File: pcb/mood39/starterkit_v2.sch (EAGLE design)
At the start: 18 parts, among them IC1 TINY85, IC2 LM2940, X1 PWRUSB

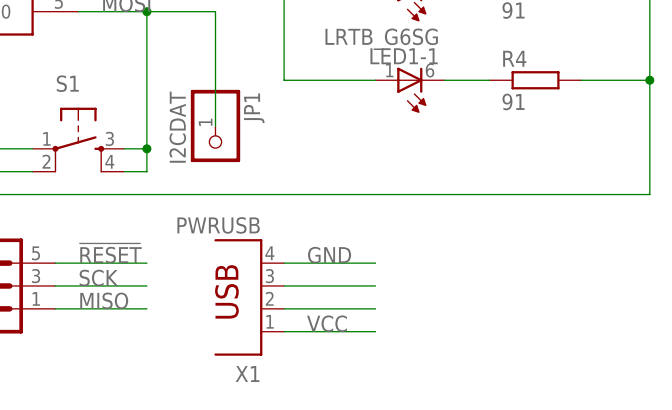
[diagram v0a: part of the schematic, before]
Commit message: add pins for USB data
those pins can be used for actually accessing the avr via USB, but it
needs some additional circuit stacked on the pin headers
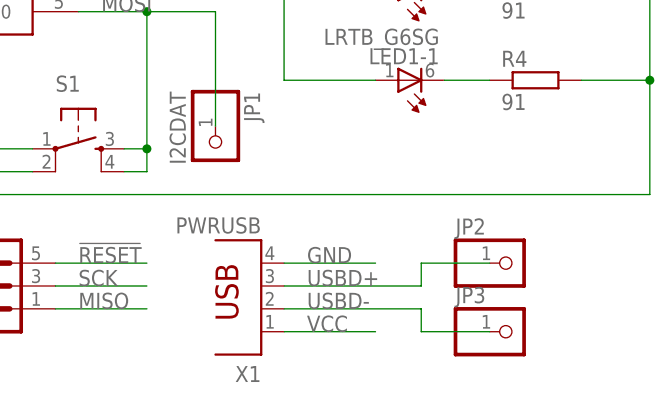
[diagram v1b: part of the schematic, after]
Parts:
- added JP2, JP3: (no value), pinhead:PINHD-1X1
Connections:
- net USBD+: now also JP2.1
- net USBD-: now also JP3.1
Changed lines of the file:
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@@
 <?xml version="1.0" encoding="utf-8"?>
 <!DOCTYPE eagle SYSTEM "eagle.dtd">
-<eagle version="6.4">
+<eagle version="6.5.0">
 <drawing>
 <settings>
@@
 <part name="S1" library="n39" deviceset="JTP-1130" device="" technology="C" value=""/>
 <part name="U$1" library="n39" deviceset="RIACON_101_2" device=""/>
+<part name="JP2" library="pinhead" deviceset="PINHD-1X1" device=""/>
+<part name="JP3" library="pinhead" deviceset="PINHD-1X1" device=""/>
 </parts>
 <sheets>
@@
 <instance part="S1" gate="S$1" x="73.66" y="50.8" rot="R270"/>
 <instance part="U$1" gate="G$1" x="-30.48" y="88.9" rot="R180"/>
+<instance part="JP2" gate="G$1" x="121.92" y="38.1"/>
+<instance part="JP3" gate="G$1" x="121.92" y="30.48"/>
 </instances>
 <busses>
@@
 <segment>
 <pinref part="X1" gate="G$1" pin="2"/>
-<wire x1="96.52" y1="33.02" x2="106.68" y2="33.02" width="0.1524" layer="91"/>
+<wire x1="96.52" y1="33.02" x2="111.76" y2="33.02" width="0.1524" layer="91"/>
+<label x="99.06" y="33.02" size="1.778" layer="95"/>
+<pinref part="JP3" gate="G$1" pin="1"/>
+<wire x1="119.38" y1="30.48" x2="111.76" y2="30.48" width="0.1524" layer="91"/>
+<wire x1="111.76" y1="30.48" x2="111.76" y2="33.02" width="0.1524" layer="91"/>
 </segment>
 </net>
@@
 <segment>
 <pinref part="X1" gate="G$1" pin="3"/>
-<wire x1="96.52" y1="35.56" x2="106.68" y2="35.56" width="0.1524" layer="91"/>
-</segment>
-</net>
+<wire x1="96.52" y1="35.56" x2="111.76" y2="35.56" width="0.1524" layer="91"/>
+<wire x1="111.76" y1="35.56" x2="111.76" y2="38.1" width="0.1524" layer="91"/>
+<wire x1="111.76" y1="38.1" x2="119.38" y2="38.1" width="0.1524" layer="91"/>
+<label x="99.06" y="35.56" size="1.778" layer="95"/>
+<pinref part="JP2" gate="G$1" pin="1"/>
+</segment>
+</net>

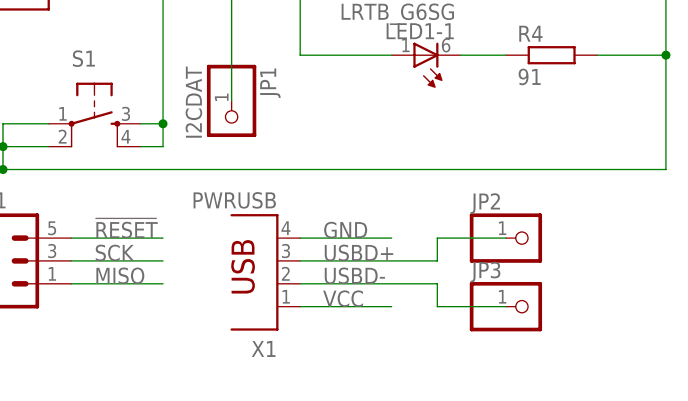
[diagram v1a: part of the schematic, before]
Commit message: replaced USB connector
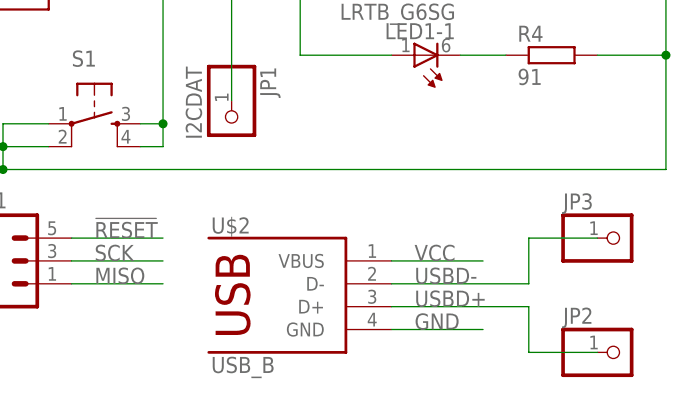
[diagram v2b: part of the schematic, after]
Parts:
- removed X1: PWRUSB, con-berg:PN61729
- added U$2: USB_B, n39:USB_B
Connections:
- net GND: now also U$2.GND; no longer X1.4
- net USBD+: now also U$2.D+; no longer X1.3
- net USBD-: now also U$2.D-; no longer X1.2
- net VCC: now also U$2.VBUS; no longer X1.1
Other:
- moved on the sheet: JP2, JP3
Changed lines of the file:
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@@
 <part name="R4" library="rcl" deviceset="R-EU_" device="R0805" value="91"/>
 <part name="SV1" library="con-ml" deviceset="ML6" device="" value="ISP"/>
-<part name="X1" library="con-berg" deviceset="PN61729" device="" value="PWRUSB"/>
 <part name="IC2" library="v-reg" deviceset="78XXS" device="" value="LM2940"/>
 <part name="C2" library="rcl" deviceset="CPOL-EU" device="E2.5-5" value="47u"/>
@@
 <part name="JP2" library="pinhead" deviceset="PINHD-1X1" device=""/>
 <part name="JP3" library="pinhead" deviceset="PINHD-1X1" device=""/>
+<part name="U$2" library="n39" deviceset="USB_B" device=""/>
 </parts>
 <sheets>
@@
 <instance part="R4" gate="G$1" x="124.46" y="58.42"/>
 <instance part="SV1" gate="1" x="63.5" y="35.56"/>
-<instance part="X1" gate="G$1" x="93.98" y="35.56" rot="R180"/>
 <instance part="IC2" gate="1" x="-5.08" y="91.44"/>
 <instance part="C2" gate="G$1" x="7.62" y="78.74"/>
@@
 <instance part="S1" gate="S$1" x="73.66" y="50.8" rot="R270"/>
 <instance part="U$1" gate="G$1" x="-30.48" y="88.9" rot="R180"/>
-<instance part="JP2" gate="G$1" x="121.92" y="38.1"/>
-<instance part="JP3" gate="G$1" x="121.92" y="30.48"/>
+<instance part="JP2" gate="G$1" x="132.08" y="25.4"/>
+<instance part="JP3" gate="G$1" x="132.08" y="38.1"/>
+<instance part="U$2" gate="G$1" x="93.98" y="30.48"/>
 </instances>
 <busses>
@@
 </segment>
 <segment>
-<pinref part="X1" gate="G$1" pin="4"/>
-<wire x1="96.52" y1="38.1" x2="106.68" y2="38.1" width="0.1524" layer="91"/>
-<label x="99.06" y="38.1" size="1.778" layer="95"/>
+<wire x1="106.68" y1="27.94" x2="116.84" y2="27.94" width="0.1524" layer="91"/>
+<label x="109.22" y="27.94" size="1.778" layer="95"/>
+<pinref part="U$2" gate="G$1" pin="GND"/>
 </segment>
 <segment>
@@
 </segment>
 <segment>
-<pinref part="X1" gate="G$1" pin="1"/>
-<wire x1="96.52" y1="30.48" x2="106.68" y2="30.48" width="0.1524" layer="91"/>
-<label x="99.06" y="30.48" size="1.778" layer="95"/>
+<wire x1="106.68" y1="35.56" x2="116.84" y2="35.56" width="0.1524" layer="91"/>
+<label x="109.22" y="35.56" size="1.778" layer="95"/>
+<pinref part="U$2" gate="G$1" pin="VBUS"/>
 </segment>
 </net>
@@
 <net name="USBD-" class="0">
 <segment>
-<pinref part="X1" gate="G$1" pin="2"/>
-<wire x1="96.52" y1="33.02" x2="111.76" y2="33.02" width="0.1524" layer="91"/>
-<label x="99.06" y="33.02" size="1.778" layer="95"/>
+<wire x1="106.68" y1="33.02" x2="121.92" y2="33.02" width="0.1524" layer="91"/>
+<label x="109.22" y="33.02" size="1.778" layer="95"/>
 <pinref part="JP3" gate="G$1" pin="1"/>
-<wire x1="119.38" y1="30.48" x2="111.76" y2="30.48" width="0.1524" layer="91"/>
-<wire x1="111.76" y1="30.48" x2="111.76" y2="33.02" width="0.1524" layer="91"/>
+<wire x1="129.54" y1="38.1" x2="121.92" y2="38.1" width="0.1524" layer="91"/>
+<wire x1="121.92" y1="38.1" x2="121.92" y2="33.02" width="0.1524" layer="91"/>
+<pinref part="U$2" gate="G$1" pin="D-"/>
 </segment>
 </net>
 <net name="USBD+" class="0">
 <segment>
-<pinref part="X1" gate="G$1" pin="3"/>
-<wire x1="96.52" y1="35.56" x2="111.76" y2="35.56" width="0.1524" layer="91"/>
-<wire x1="111.76" y1="35.56" x2="111.76" y2="38.1" width="0.1524" layer="91"/>
-<wire x1="111.76" y1="38.1" x2="119.38" y2="38.1" width="0.1524" layer="91"/>
-<label x="99.06" y="35.56" size="1.778" layer="95"/>
+<wire x1="106.68" y1="30.48" x2="121.92" y2="30.48" width="0.1524" layer="91"/>
+<wire x1="121.92" y1="30.48" x2="121.92" y2="25.4" width="0.1524" layer="91"/>
+<wire x1="121.92" y1="25.4" x2="129.54" y2="25.4" width="0.1524" layer="91"/>
+<label x="109.22" y="30.48" size="1.778" layer="95"/>
 <pinref part="JP2" gate="G$1" pin="1"/>
-</segment>
-</net>
+<pinref part="U$2" gate="G$1" pin="D+"/>
+</segment>
+</net>

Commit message: replace voltage regulator
this saves one capacitor and lots of space
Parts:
- removed C3: 470n, rcl:C-EUC0805
- C2: value 47u -> 2.2u; device rcl:CPOL-EUE2.5-5 -> rcl:CPOL-EUE2-5
- IC2: value LM2940 -> LP2950; device v-reg:78XXS -> v-reg:LP2950ACZ-5.0
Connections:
- net GND: no longer C3.2
- net V+: no longer C3.1
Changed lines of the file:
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@@
 <part name="R4" library="rcl" deviceset="R-EU_" device="R0805" value="91"/>
 <part name="SV1" library="con-ml" deviceset="ML6" device="" value="ISP"/>
-<part name="IC2" library="v-reg" deviceset="78XXS" device="" value="LM2940"/>
-<part name="C2" library="rcl" deviceset="CPOL-EU" device="E2.5-5" value="47u"/>
-<part name="C3" library="rcl" deviceset="C-EU" device="C0805" value="470n"/>
+<part name="IC2" library="v-reg" deviceset="LP2950?*" device="ACZ" technology="-5.0" value="LP2950"/>
+<part name="C2" library="rcl" deviceset="CPOL-EU" device="E2-5" value="2.2u"/>
 <part name="R5" library="n39" deviceset="ALPS_RK09K113" device=""/>
 <part name="JP1" library="pinhead" deviceset="PINHD-1X1" device="" value="I2CDAT"/>
@@
 <instance part="R4" gate="G$1" x="124.46" y="58.42"/>
 <instance part="SV1" gate="1" x="63.5" y="35.56"/>
-<instance part="IC2" gate="1" x="-5.08" y="91.44"/>
+<instance part="IC2" gate="G$1" x="-5.08" y="91.44"/>
 <instance part="C2" gate="G$1" x="7.62" y="78.74"/>
-<instance part="C3" gate="G$1" x="-17.78" y="78.74"/>
 <instance part="R5" gate="R$1" x="83.82" y="91.44" rot="MR270"/>
 <instance part="JP1" gate="G$1" x="88.9" y="50.8" rot="R270"/>
@@
 <junction x="137.16" y="58.42"/>
 <junction x="137.16" y="68.58"/>
-<pinref part="IC2" gate="1" pin="GND"/>
-<wire x1="-17.78" y1="45.72" x2="-5.08" y2="45.72" width="0.1524" layer="91"/>
+<pinref part="IC2" gate="G$1" pin="GND"/>
+<wire x1="-22.86" y1="45.72" x2="-5.08" y2="45.72" width="0.1524" layer="91"/>
 <wire x1="-5.08" y1="45.72" x2="7.62" y2="45.72" width="0.1524" layer="91"/>
 <wire x1="7.62" y1="45.72" x2="15.24" y2="45.72" width="0.1524" layer="91"/>
@@
 <wire x1="7.62" y1="73.66" x2="7.62" y2="45.72" width="0.1524" layer="91"/>
 <junction x="7.62" y="45.72"/>
-<pinref part="C3" gate="G$1" pin="2"/>
-<wire x1="-17.78" y1="73.66" x2="-17.78" y2="45.72" width="0.1524" layer="91"/>
-<junction x="-17.78" y="45.72"/>
 <pinref part="LED2" gate="G$1" pin="C"/>
 <wire x1="38.1" y1="48.26" x2="38.1" y2="45.72" width="0.1524" layer="91"/>
@@
 <wire x1="-25.4" y1="88.9" x2="-22.86" y2="88.9" width="0.1524" layer="91"/>
 <wire x1="-22.86" y1="88.9" x2="-22.86" y2="45.72" width="0.1524" layer="91"/>
-<wire x1="-22.86" y1="45.72" x2="-17.78" y2="45.72" width="0.1524" layer="91"/>
 </segment>
 <segment>
@@
 <wire x1="15.24" y1="91.44" x2="15.24" y2="93.98" width="0.1524" layer="91"/>
 <junction x="15.24" y="91.44"/>
-<pinref part="IC2" gate="1" pin="OUT"/>
+<pinref part="IC2" gate="G$1" pin="OUT"/>
 <wire x1="2.54" y1="91.44" x2="7.62" y2="91.44" width="0.1524" layer="91"/>
 <pinref part="C2" gate="G$1" pin="+"/>
@@
 <net name="V+" class="1">
 <segment>
-<pinref part="IC2" gate="1" pin="IN"/>
-<pinref part="C3" gate="G$1" pin="1"/>
-<wire x1="-17.78" y1="91.44" x2="-12.7" y2="91.44" width="0.1524" layer="91"/>
-<wire x1="-17.78" y1="81.28" x2="-17.78" y2="91.44" width="0.1524" layer="91"/>
+<pinref part="IC2" gate="G$1" pin="IN"/>
 <label x="-15.24" y="91.44" size="1.778" layer="95"/>
-<wire x1="-25.4" y1="91.44" x2="-17.78" y2="91.44" width="0.1524" layer="91"/>
-<junction x="-17.78" y="91.44"/>
+<wire x1="-25.4" y1="91.44" x2="-12.7" y2="91.44" width="0.1524" layer="91"/>
 <pinref part="U$1" gate="G$1" pin="2"/>
 </segment>

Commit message: routing almost done
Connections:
- net GND: now also R5.E; no longer R5.A
- net VCC: now also R5.A; no longer R5.E
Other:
- moved on the sheet: R5
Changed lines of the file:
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@@
 <grid distance="0.1" unitdist="inch" unit="inch" style="lines" multiple="1" display="no" altdistance="0.01" altunitdist="inch" altunit="inch"/>
 <layers>
-<layer number="1" name="Top" color="4" fill="1" visible="yes" active="no"/>
-<layer number="16" name="Bottom" color="1" fill="1" visible="yes" active="no"/>
-<layer number="17" name="Pads" color="2" fill="1" visible="yes" active="no"/>
-<layer number="18" name="Vias" color="2" fill="1" visible="yes" active="no"/>
-<layer number="19" name="Unrouted" color="6" fill="1" visible="yes" active="no"/>
-<layer number="20" name="Dimension" color="15" fill="1" visible="yes" active="no"/>
-<layer number="21" name="tPlace" color="7" fill="1" visible="yes" active="no"/>
-<layer number="22" name="bPlace" color="7" fill="1" visible="yes" active="no"/>
-<layer number="23" name="tOrigins" color="15" fill="1" visible="yes" active="no"/>
-<layer number="24" name="bOrigins" color="15" fill="1" visible="yes" active="no"/>
-<layer number="25" name="tNames" color="7" fill="1" visible="yes" active="no"/>
-<layer number="26" name="bNames" color="7" fill="1" visible="yes" active="no"/>
-<layer number="27" name="tValues" color="7" fill="1" visible="yes" active="no"/>
-<layer number="28" name="bValues" color="7" fill="1" visible="yes" active="no"/>
+<layer number="1" name="Top" color="4" fill="1" visible="no" active="no"/>
+<layer number="16" name="Bottom" color="1" fill="1" visible="no" active="no"/>
+<layer number="17" name="Pads" color="2" fill="1" visible="no" active="no"/>
+<layer number="18" name="Vias" color="2" fill="1" visible="no" active="no"/>
+<layer number="19" name="Unrouted" color="6" fill="1" visible="no" active="no"/>
+<layer number="20" name="Dimension" color="15" fill="1" visible="no" active="no"/>
+<layer number="21" name="tPlace" color="7" fill="1" visible="no" active="no"/>
+<layer number="22" name="bPlace" color="7" fill="1" visible="no" active="no"/>
+<layer number="23" name="tOrigins" color="15" fill="1" visible="no" active="no"/>
+<layer number="24" name="bOrigins" color="15" fill="1" visible="no" active="no"/>
+<layer number="25" name="tNames" color="7" fill="1" visible="no" active="no"/>
+<layer number="26" name="bNames" color="7" fill="1" visible="no" active="no"/>
+<layer number="27" name="tValues" color="7" fill="1" visible="no" active="no"/>
+<layer number="28" name="bValues" color="7" fill="1" visible="no" active="no"/>
 <layer number="29" name="tStop" color="7" fill="3" visible="no" active="no"/>
 <layer number="30" name="bStop" color="7" fill="6" visible="no" active="no"/>
@@
 <layer number="35" name="tGlue" color="7" fill="4" visible="no" active="no"/>
 <layer number="36" name="bGlue" color="7" fill="5" visible="no" active="no"/>
-<layer number="37" name="tTest" color="7" fill="1" visible="yes" active="no"/>
-<layer number="38" name="bTest" color="7" fill="1" visible="yes" active="no"/>
+<layer number="37" name="tTest" color="7" fill="1" visible="no" active="no"/>
+<layer number="38" name="bTest" color="7" fill="1" visible="no" active="no"/>
 <layer number="39" name="tKeepout" color="4" fill="11" visible="no" active="no"/>
 <layer number="40" name="bKeepout" color="1" fill="11" visible="no" active="no"/>
@@
 <layer number="44" name="Drills" color="7" fill="1" visible="no" active="no"/>
 <layer number="45" name="Holes" color="7" fill="1" visible="no" active="no"/>
-<layer number="46" name="Milling" color="3" fill="1" visible="yes" active="no"/>
-<layer number="47" name="Measures" color="7" fill="1" visible="yes" active="no"/>
-<layer number="48" name="Document" color="7" fill="1" visible="yes" active="no"/>
-<layer number="49" name="Reference" color="7" fill="1" visible="yes" active="no"/>
-<layer number="51" name="tDocu" color="7" fill="1" visible="yes" active="no"/>
-<layer number="52" name="bDocu" color="7" fill="1" visible="yes" active="no"/>
+<layer number="46" name="Milling" color="3" fill="1" visible="no" active="no"/>
+<layer number="47" name="Measures" color="7" fill="1" visible="no" active="no"/>
+<layer number="48" name="Document" color="7" fill="1" visible="no" active="no"/>
+<layer number="49" name="Reference" color="7" fill="1" visible="no" active="no"/>
+<layer number="51" name="tDocu" color="7" fill="1" visible="no" active="no"/>
+<layer number="52" name="bDocu" color="7" fill="1" visible="no" active="no"/>
 <layer number="91" name="Nets" color="2" fill="1" visible="yes" active="yes"/>
 <layer number="92" name="Busses" color="1" fill="1" visible="yes" active="yes"/>
@@
 <instance part="IC2" gate="G$1" x="-5.08" y="91.44"/>
 <instance part="C2" gate="G$1" x="7.62" y="78.74"/>
-<instance part="R5" gate="R$1" x="83.82" y="91.44" rot="MR270"/>
+<instance part="R5" gate="R$1" x="73.66" y="91.44" rot="MR90"/>
 <instance part="JP1" gate="G$1" x="88.9" y="50.8" rot="R270"/>
-<instance part="GND2" gate="1" x="91.44" y="86.36"/>
+<instance part="GND2" gate="1" x="91.44" y="81.28"/>
 <instance part="LED2" gate="G$1" x="38.1" y="53.34"/>
 <instance part="R6" gate="G$1" x="30.48" y="58.42"/>
@@
 </segment>
 <segment>
-<pinref part="R5" gate="R$1" pin="A"/>
-<wire x1="88.9" y1="91.44" x2="91.44" y2="91.44" width="0.1524" layer="91"/>
-<wire x1="91.44" y1="91.44" x2="91.44" y2="88.9" width="0.1524" layer="91"/>
 <pinref part="GND2" gate="1" pin="GND"/>
+<wire x1="91.44" y1="83.82" x2="91.44" y2="91.44" width="0.1524" layer="91"/>
+<pinref part="R5" gate="R$1" pin="E"/>
+<wire x1="91.44" y1="91.44" x2="78.74" y2="91.44" width="0.1524" layer="91"/>
 </segment>
 </net>
@@
 <wire x1="7.62" y1="81.28" x2="7.62" y2="91.44" width="0.1524" layer="91"/>
 <junction x="7.62" y="91.44"/>
-<pinref part="R5" gate="R$1" pin="E"/>
 <wire x1="22.86" y1="91.44" x2="27.94" y2="91.44" width="0.1524" layer="91"/>
 <pinref part="R1" gate="G$1" pin="1"/>
-<wire x1="27.94" y1="91.44" x2="78.74" y2="91.44" width="0.1524" layer="91"/>
 <wire x1="27.94" y1="88.9" x2="27.94" y2="91.44" width="0.1524" layer="91"/>
-<junction x="27.94" y="91.44"/>
 <wire x1="22.86" y1="68.58" x2="22.86" y2="58.42" width="0.1524" layer="91"/>
 <pinref part="R6" gate="G$1" pin="1"/>
 <wire x1="22.86" y1="58.42" x2="25.4" y2="58.42" width="0.1524" layer="91"/>
 <junction x="22.86" y="68.58"/>
+<pinref part="R5" gate="R$1" pin="A"/>
+<wire x1="68.58" y1="91.44" x2="27.94" y2="91.44" width="0.1524" layer="91"/>
+<junction x="27.94" y="91.44"/>
 </segment>
 <segment>
@@
 <label x="76.2" y="71.12" size="1.778" layer="95"/>
 <pinref part="R5" gate="R$1" pin="S"/>
-<wire x1="83.82" y1="86.36" x2="83.82" y2="71.12" width="0.1524" layer="91"/>
-</segment>
-<segment>
+<wire x1="73.66" y1="96.52" x2="73.66" y2="99.06" width="0.1524" layer="91"/>
+<wire x1="73.66" y1="99.06" x2="83.82" y2="99.06" width="0.1524" layer="91"/>
+<wire x1="83.82" y1="99.06" x2="83.82" y2="71.12" width="0.1524" layer="91"/>
+</segment>
+<segment>
